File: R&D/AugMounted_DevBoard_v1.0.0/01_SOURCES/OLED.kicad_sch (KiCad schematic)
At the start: 6 parts, among them J3 J_FH43BW-61S-0.2SHW, U4 U_TXB0108PWR, U5 U_TXB0108PWR, U6 U_TXB0108PWR, U7 U_LP3987H-18B5F, U8 U_TPS61087DRCR

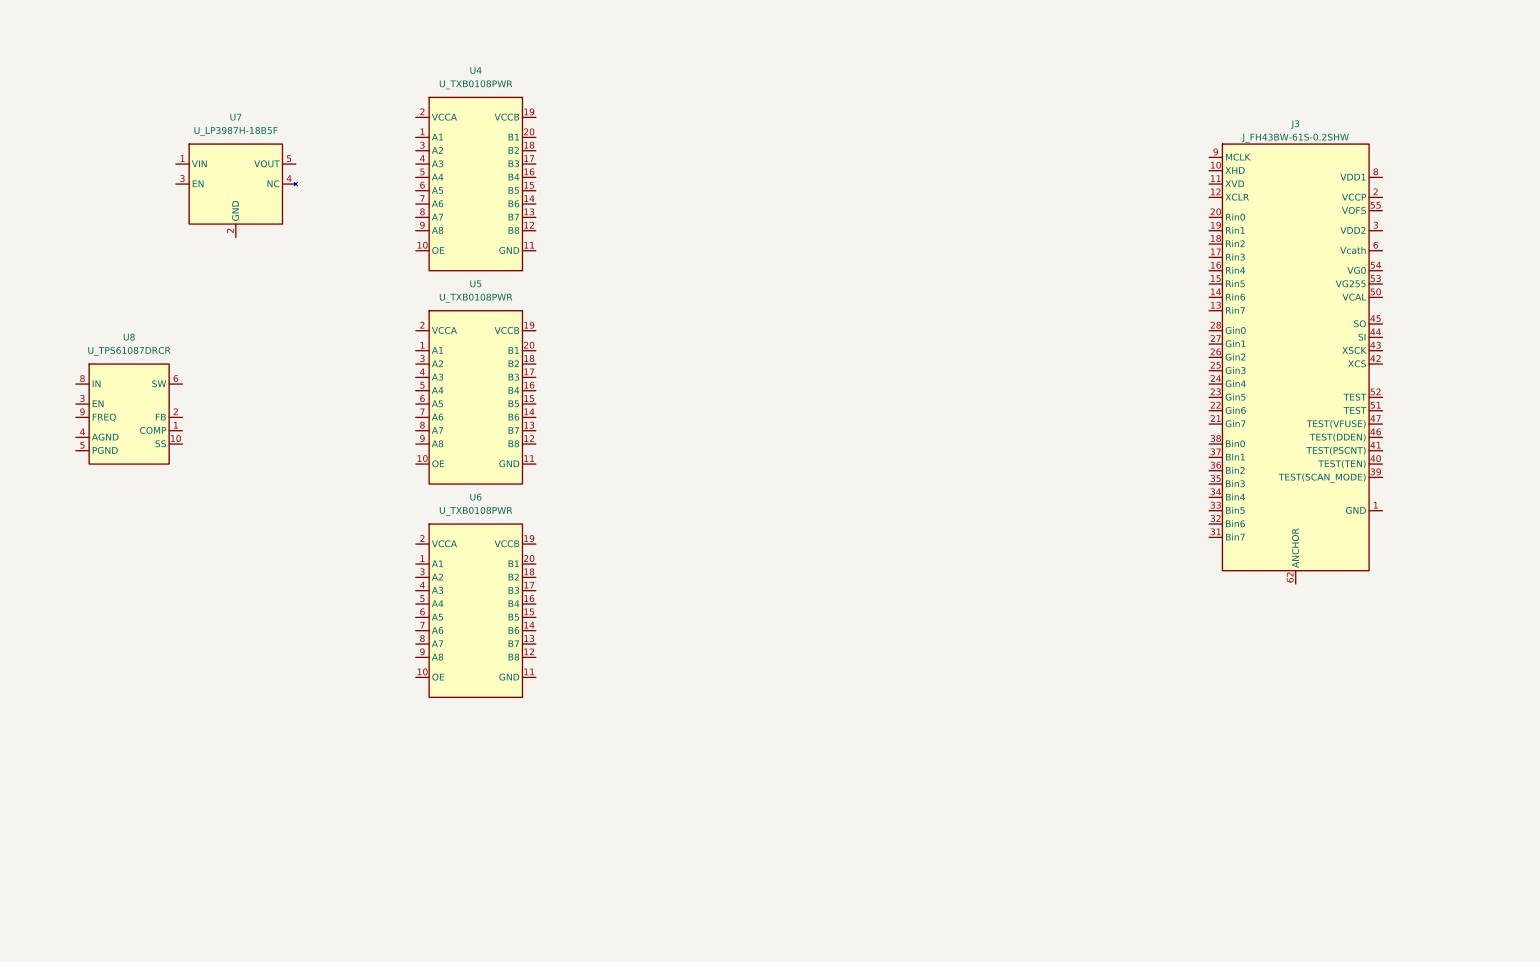
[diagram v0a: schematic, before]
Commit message: Oled driving circuit done, need to connect everything to the ESP32
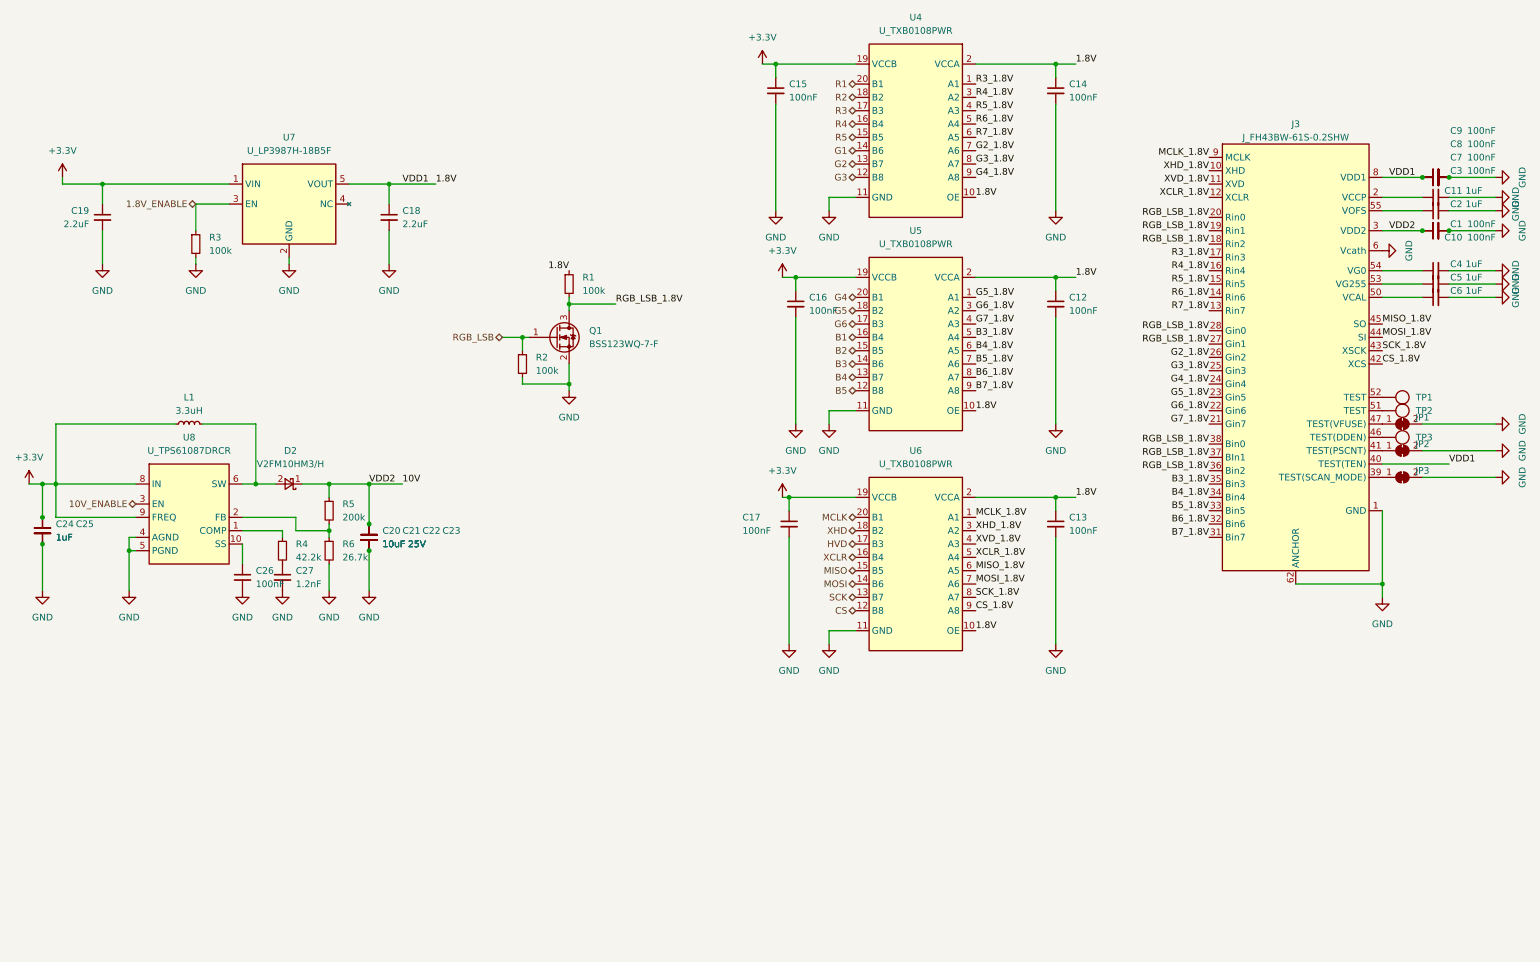
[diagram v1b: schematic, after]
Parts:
- added C1, C10, C12, C13, C14, C15, C16, C17, C26, C3, C7, C8, C9: C_0603_100nF_100V_X7R_10%, .mounted-lib:C_0603_1608Metric, symbol .mounted-lib:C_0603_100nF_100V_X7R_10%
- added C11, C2, C24, C25, C4, C5, C6: C_0805_1uF_100V_X7S_20%, .mounted-lib:C_0805_1608Metric, symbol .mounted-lib:C_0805_1uF_100V_X7S_20%
- added C18, C19: C_0805_2.2uF_25V_X7R_20%, .mounted-lib:C_0805_1608Metric, symbol .mounted-lib:C_0805_2.2uF_25V_X7R_20%
- added C20, C21, C22, C23: C_1206_10uF_25V_X7R_10%, .mounted-lib:C_1206_3216Metric, symbol .mounted-lib:C_1206_10uF_25V_X7R_10%
- added C27: C_0603_1.2nF_100V_X7R_5%, .mounted-lib:C_0603_1608Metric, symbol .mounted-lib:C_0603_1.2nF_100V_X7R_5%
- added D2: D_V2FM10HM3/H, .mounted-lib:D_SMF_VISHAY, symbol .mounted-lib:D_V2FM10HM3/H
- added JP1, JP2, JP3: SolderJumper_2_Bridged, Jumper:SolderJumper-2_P1.3mm_Bridged_RoundedPad1.0x1.5mm, symbol Jumper:SolderJumper_2_Bridged
- added L1: L_7447789003, symbol .mounted-lib:L_7447789003
- added Q1: Q_BSS123WQ-7-F, .mounted-lib:SOT-323_SC-70_DIODES_INC, symbol .mounted-lib:Q_BSS123WQ-7-F
- added R1, R2, R3: R_0603_100k_1%_0.1W, .mounted-lib:R_0603_1608Metric, symbol .mounted-lib:R_0603_100k_1%_0.1W
- added R4: R_0603_42.2k_1%_0.1W, .mounted-lib:R_0603_1608Metric, symbol .mounted-lib:R_0603_42.2k_1%_0.1W
- added R5: R_0603_200k_1%_0.1W, .mounted-lib:R_0603_1608Metric, symbol .mounted-lib:R_0603_200k_1%_0.1W
- added R6: R_0603_26.7k_1%_0.1W, .mounted-lib:R_0603_1608Metric, symbol .mounted-lib:R_0603_26.7k_1%_0.1W
- added TP1, TP2, TP3: TESTPOINT_1MM, .mounted-lib:TESTPOINT_1MM, symbol .mounted-lib:TESTPOINT_1MM
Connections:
- net R3_1.8V: now reaches U4.1 (A1)
- net R3_1.8V: now also J3.17 (Rin3)
- net 1.8V: now reaches U4.10 (OE)
- net 1.8V: now also J3.29 (VDD1), J3.40 (TEST(TEN)), J3.49 (VDD1), J3.8 (VDD1), U4.2 (VCCA), U5.10 (OE), U5.2 (VCCA), U6.10 (OE), U6.2 (VCCA), U7.5 (VOUT), C12.1, C13.1, C14.1, C18.1, C3.1, C7.1, C8.1, C9.1, R1.1
- net GND: now reaches U4.11 (GND)
- net GND: now also J3.1 (GND), J3.30 (GND), J3.4 (GND), J3.48 (GND), J3.5 (GND), J3.56 (Vcath), J3.57 (GND), J3.58 (GND), J3.6 (Vcath), J3.61 (GND), J3.62 (ANCHOR), J3.63 (ANCHOR), J3.7 (GND), U5.11 (GND), U6.11 (GND), U7.2 (GND), U8.4 (AGND), U8.5 (PGND), C1.2, C10.2, C11.2, C12.2, C13.2, C14.2, C15.2, C16.2, C17.2, C18.2, C19.2, C2.2, C20.2, C21.2, C22.2, C23.2, C24.2, C25.2, C26.2, C27.2, C3.2, C4.2, C5.2, C6.2, C7.2, C8.2, C9.2, JP1.2 (B), JP2.2 (B), JP3.2 (B), Q1.2 (S), R2.2, R3.2, R6.2
- net G3: now reaches U4.12 (B8)
- net G2: now reaches U4.13 (B7)
- net G1: now reaches U4.14 (B6)
- net R5: now reaches U4.15 (B5)
- net R4: now reaches U4.16 (B4)
- net R3: now reaches U4.17 (B3)
- net R2: now reaches U4.18 (B2)
- net +3.3V: now reaches U4.19 (VCCB)
- net +3.3V: now also U5.19 (VCCB), U6.19 (VCCB), U7.1 (VIN), U8.8 (IN), U8.9 (FREQ), C15.1, C16.1, C17.1, C19.1, C24.1, C25.1, L1.1
- net R1: now reaches U4.20 (B1)
- net R4_1.8V: now reaches U4.3 (A2)
- net R4_1.8V: now also J3.16 (Rin4)
- net R5_1.8V: now reaches U4.4 (A3)
- net R5_1.8V: now also J3.15 (Rin5)
- net R6_1.8V: now reaches U4.5 (A4)
- net R6_1.8V: now also J3.14 (Rin6)
- net R7_1.8V: now reaches U4.6 (A5)
- net R7_1.8V: now also J3.13 (Rin7)
- net G2_1.8V: now reaches U4.7 (A6)
- net G2_1.8V: now also J3.26 (Gin2)
- net G3_1.8V: now reaches U4.8 (A7)
- net G3_1.8V: now also J3.25 (Gin3)
- net G4_1.8V: now reaches U4.9 (A8)
- net G4_1.8V: now also J3.24 (Gin4)
- net G5_1.8V: now reaches U5.1 (A1)
- net G5_1.8V: now also J3.23 (Gin5)
- net B5: now reaches U5.12 (B8)
- net B4: now reaches U5.13 (B7)
- net B3: now reaches U5.14 (B6)
- net B2: now reaches U5.15 (B5)
- net B1: now reaches U5.16 (B4)
- net G6: now reaches U5.17 (B3)
- net G5: now reaches U5.18 (B2)
- net G4: now reaches U5.20 (B1)
- net G6_1.8V: now reaches U5.3 (A2)
- net G6_1.8V: now also J3.22 (Gin6)
- net G7_1.8V: now reaches U5.4 (A3)
- net G7_1.8V: now also J3.21 (Gin7)
- net B3_1.8V: now reaches U5.5 (A4)
- net B3_1.8V: now also J3.35 (Bin3)
- net B4_1.8V: now reaches U5.6 (A5)
- net B4_1.8V: now also J3.34 (Bin4)
- net B5_1.8V: now reaches U5.7 (A6)
- net B5_1.8V: now also J3.33 (Bin5)
- net B6_1.8V: now reaches U5.8 (A7)
- net B6_1.8V: now also J3.32 (Bin6)
- net B7_1.8V: now reaches U5.9 (A8)
- net B7_1.8V: now also J3.31 (Bin7)
- net at U8.1 (COMP): now also R4.1
- net at U8.10 (SS): now also C26.1
- net at U8.2 (FB): now also R5.2, R6.1
- net 10V_ENABLE: now reaches U8.3 (EN)
- net at U8.6 (SW), U8.7 (SW): now also D2.2 (A), L1.2
- net 1.8V_ENABLE: now reaches U7.3 (EN)
- net 1.8V_ENABLE: now also R3.1
- net MCLK_1.8V: now reaches U6.1 (A1)
- net MCLK_1.8V: now also J3.9 (MCLK)
- net CS: now reaches U6.12 (B8)
- net SCK: now reaches U6.13 (B7)
- net MOSI: now reaches U6.14 (B6)
- net MISO: now reaches U6.15 (B5)
- net XCLR: now reaches U6.16 (B4)
- net HVD: now reaches U6.17 (B3)
- net XHD: now reaches U6.18 (B2)
- net MCLK: now reaches U6.20 (B1)
- net XHD_1.8V: now reaches U6.3 (A2)
- net XHD_1.8V: now also J3.10 (XHD)
- net XVD_1.8V: now reaches U6.4 (A3)
- net XVD_1.8V: now also J3.11 (XVD)
- net XCLR_1.8V: now reaches U6.5 (A4)
- net XCLR_1.8V: now also J3.12 (XCLR)
- net MISO_1.8V: now reaches U6.6 (A5)
- net MISO_1.8V: now also J3.45 (SO)
- net MOSI_1.8V: now reaches U6.7 (A6)
- net MOSI_1.8V: now also J3.44 (SI)
- net SCK_1.8V: now reaches U6.8 (A7)
- net SCK_1.8V: now also J3.43 (XSCK)
- net CS_1.8V: now reaches U6.9 (A8)
- net CS_1.8V: now also J3.42 (XCS)
- net RGB_LSB_1.8V: now reaches J3.18 (Rin2)
- net RGB_LSB_1.8V: now also J3.19 (Rin1), J3.20 (Rin0), J3.27 (Gin1), J3.28 (Gin0), J3.36 (Bin2), J3.37 (BIn1), J3.38 (Bin0), Q1.3 (D), R1.2
- net at J3.2 (VCCP), J3.60 (VCCP): now also C11.1
- net 10V: now reaches J3.3 (VDD2), J3.59 (VDD2)
- net 10V: now also C1.1, C10.1, C20.1, C21.1, C22.1, C23.1, D2.1 (K), R5.1
- net at J3.39 (TEST(SCAN_MODE)): now also JP3.1 (A)
- net at J3.41 (TEST(PSCNT)): now also JP2.1 (A)
- net at J3.46 (TEST(DDEN)): now also TP3.1
- net at J3.47 (TEST(VFUSE)): now also JP1.1 (A)
- net at J3.50 (VCAL): now also C6.1
- net at J3.51 (TEST): now also TP2.1
- net at J3.52 (TEST): now also TP1.1
- net at J3.53 (VG255): now also C5.1
- net at J3.54 (VG0): now also C4.1
- net at J3.55 (VOFS): now also C2.1
- new net: C27.1, R4.2
- new net RGB_LSB: Q1.1 (G), R2.1
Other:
- moved on the sheet: U4, U5, U6, U7, U8

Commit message: Schematic 90% done
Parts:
- removed C18, C19: C_0805_2.2uF_25V_X7R_20%, .mounted-lib:C_0805_1608Metric, symbol .mounted-lib:C_0805_2.2uF_25V_X7R_20%
- removed C20, C21, C22, C23: C_1206_10uF_25V_X7R_10%, .mounted-lib:C_1206_3216Metric, symbol .mounted-lib:C_1206_10uF_25V_X7R_10%
- removed C24, C25: C_0805_1uF_100V_X7S_20%, .mounted-lib:C_0805_1608Metric, symbol .mounted-lib:C_0805_1uF_100V_X7S_20%
- removed C26: C_0603_100nF_100V_X7R_10%, .mounted-lib:C_0603_1608Metric, symbol .mounted-lib:C_0603_100nF_100V_X7R_10%
- removed C27: C_0603_1.2nF_100V_X7R_5%, .mounted-lib:C_0603_1608Metric, symbol .mounted-lib:C_0603_1.2nF_100V_X7R_5%
- removed D2: D_V2FM10HM3/H, .mounted-lib:D_SMF_VISHAY, symbol .mounted-lib:D_V2FM10HM3/H
- removed L1: L_7447789003, symbol .mounted-lib:L_7447789003
- removed R3: R_0603_100k_1%_0.1W, .mounted-lib:R_0603_1608Metric, symbol .mounted-lib:R_0603_100k_1%_0.1W
- removed R4: R_0603_42.2k_1%_0.1W, .mounted-lib:R_0603_1608Metric, symbol .mounted-lib:R_0603_42.2k_1%_0.1W
- removed R5: R_0603_200k_1%_0.1W, .mounted-lib:R_0603_1608Metric, symbol .mounted-lib:R_0603_200k_1%_0.1W
- removed R6: R_0603_26.7k_1%_0.1W, .mounted-lib:R_0603_1608Metric, symbol .mounted-lib:R_0603_26.7k_1%_0.1W
- removed U7: U_LP3987H-18B5F, .mounted-lib:SOT-23-5_LOW_POWER, symbol .mounted-lib:U_LP3987H-18B5F
- removed U8: U_TPS61087DRCR, .mounted-lib:PVSON-N10_TEXAS_INSTRUMENTS, symbol .mounted-lib:U_TPS61087DRCR
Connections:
- net 1.8V: no longer C12.1, C13.1, C14.1, C3.1, C7.1, C8.1, C9.1, J3.29 (VDD1), J3.40 (TEST(TEN)), J3.49 (VDD1), J3.8 (VDD1), R1.1, U4.2 (VCCA), U5.2 (VCCA), U6.2 (VCCA)
- net 10V renamed VDD2
- new net +1V8: C12.1, C13.1, C14.1, R1.1, U4.2 (VCCA), U5.2 (VCCA), U6.2 (VCCA)
- new net 1.8V_LCD: C3.1, C7.1, C8.1, C9.1, J3.29 (VDD1), J3.40 (TEST(TEN)), J3.49 (VDD1), J3.8 (VDD1)
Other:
- moved on the sheet: Q1, R1, R2
